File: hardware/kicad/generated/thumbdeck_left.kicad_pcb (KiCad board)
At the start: 4 copper layers, 75 x 98 mm, 85 parts, among them J2 FFC16, SW1 SNAP7, SW10 SNAP7, SW11 SNAP7, SW12 SNAP7, SW13 SNAP7, SW14 SNAP7, SW15 SNAP7, SW16 SNAP7, SW17 SNAP7, SW18 SNAP7, SW19 SNAP7, SW2 SNAP7, SW20 SNAP7, SW21 SNAP7, SW22 SNAP7, SW23 SNAP7, SW24 SNAP7, SW25 SNAP7, SW26 SNAP7, SW27 SNAP7, SW28 SNAP7, SW29 SNAP7, SW3 SNAP7, SW30 SNAP7, SW31 SNAP7, SW32 SNAP7, SW33 SNAP7, SW34 SNAP7, SW35 SNAP7, SW36 SNAP7, SW37 SNAP7, SW38 SNAP7, SW39 SNAP7, SW4 SNAP7, SW40 SNAP7, SW41 SNAP7, SW42 SNAP7, SW5 SNAP7, SW6 SNAP7, SW7 SNAP7, SW8 SNAP7, SW9 SNAP7

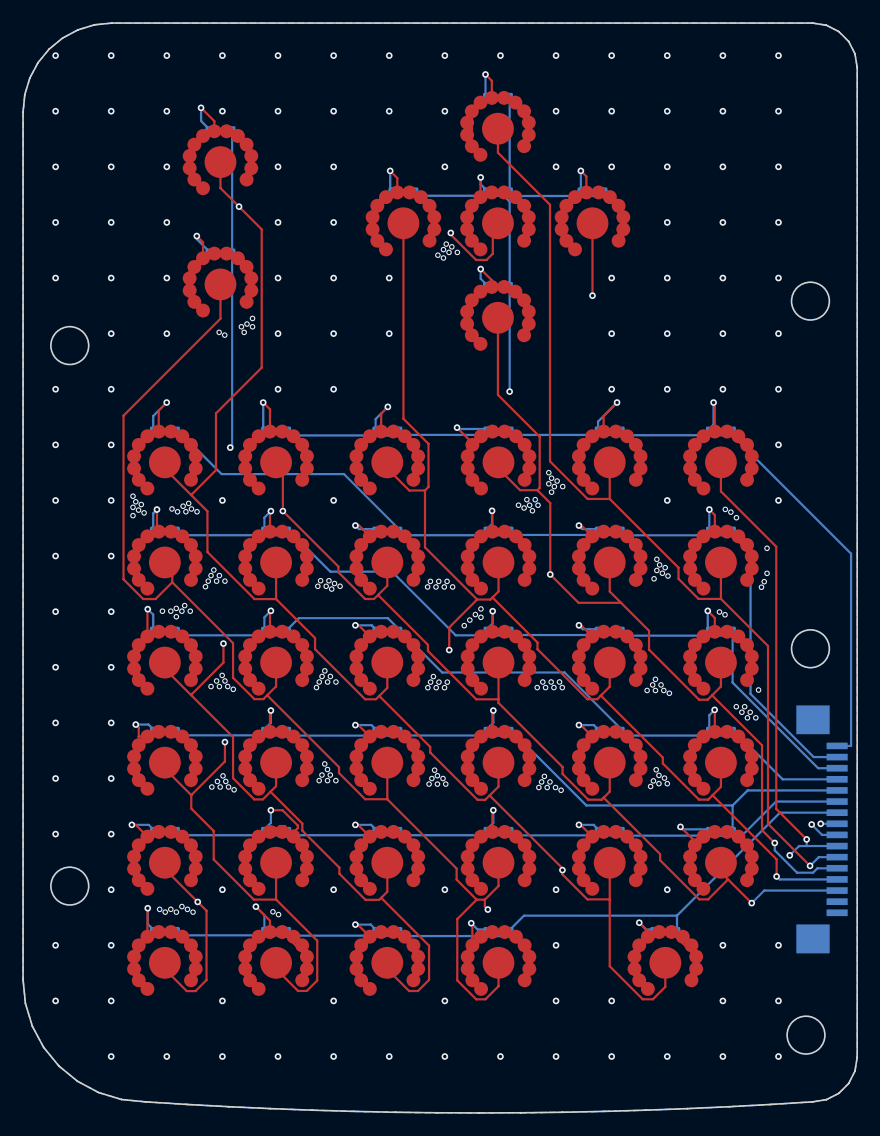
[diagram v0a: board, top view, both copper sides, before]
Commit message: v0.21: right-grip ThinkPad-style pointing nub — Bean-architecture TMAG5273 hall sensor
The right top zone mirrors the left cluster: PgUp/PgDn at the mouse-button
mirror, and a rate-control pointing nub at the exact D-pad mirror (32.3, 79.0).
Architecture per the Ploopy Bean (CERN-OHL-S v2, credited): a TMAG5273A1 I2C
hall sensor (C3716049, SOT-23-6, machine-placed SMT on the back) reads a
O4x2 N52 magnet in a printed flexure spring through the 1.6mm FR4; firmware
maps deflection to cursor VELOCITY (quadratic curve + deadzone + remainder).
An ALPS RKJXV gimbal variant was fully implemented first and rejected — the
11.2mm module body protruded through the face; recorded in the design log.

- board: U4 + R26/R27 pullups + C8 on the reserved TP6-8 I2C nets (P0.05/28/29),
  all-SMT again (71/43 placements); reworked USB In2 lane elbow; pre-placed GND
  escapes for U1.21/24 (fan-out walled their pour blob in deterministically);
  both boards routed 0 violations / 0 unconnected
- firmware: in-tree Zephyr module tmag5273_nub (Apache-2.0, register map from
  the upstream Zephyr driver, NOT the Bean's GPL QMK): 100Hz poll, boot zero
  calibration, DT-tunable curve, pm_device sleep hook (continuous mode would
  drain ~2.3mA through ZMK deep sleep); matrix stays 78 keys
- CAD: flat face with a O10 aperture; prints 8+9 = nub_spring (flange + spiral
  arms + legs clamped by the lid counterbore at 0.05 preload) and TPU nub_cap
  (4.25mm proud); 221 bodies, 0 collisions; GLB includes the nub
- docs: BOM/assembly/README/design-log rewritten for the nub; magnet polarity
  procedure; CI marked stale pending a v0.21 re-run; 78-key counts restored
- verified by a 17-agent adversarial review: fixed the spigot z-stack (cap had
  0.15mm engagement), the unclamped spring flange, and the sensor sleep drain

Co-Authored-By: Claude Fable 5 <noreply@anthropic.com>
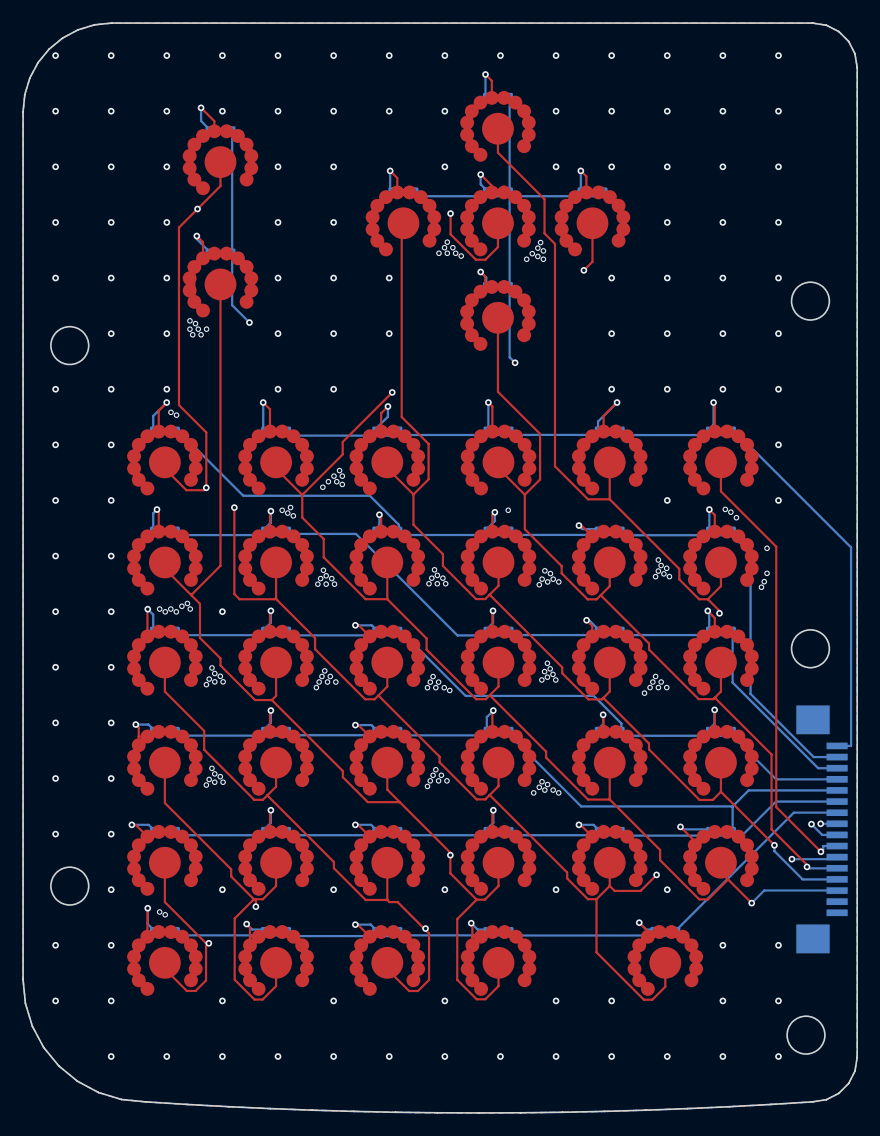
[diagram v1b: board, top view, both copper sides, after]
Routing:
- net COL8: track 167.0 -> 180.5 mm, vias 3 -> 2
- net ROW8: track 99.5 -> 90.3 mm
- net DN_L29: track 22.2 -> 17.7 mm
- net COL7: track 171.5 -> 167.6 mm, vias 3 -> 2
- net COL6: track 227.5 -> 223.8 mm, vias 2 -> 3
- net COL9: track 195.2 -> 191.7 mm
- net COL5: track 214.0 -> 217.3 mm, vias 5 -> 6
- net DN_L34: track 19.4 -> 17.3 mm
- net ROW6: track 66.4 -> 65.6 mm
- net DN_L38: track 17.4 -> 16.6 mm
- net DN_L10: track 17.4 -> 16.8 mm
- net DN_L14: track 17.2 -> 16.6 mm
- net DN_L36: track 16.9 -> 17.4 mm
- net GND: vias 304 -> 261

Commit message: v0.22: true-mirror page keys + genuine-TrackPoint-cap nub mount
Two feedback items on the v0.21 print:

- PGUP/PGDN move to the TRUE mouse-button mirror x=57.25 (the F10|DEL gap,
  mirroring the left pair's ESC|F1 gap; was 45.7, "above F9"). v0.21's
  blocker was a face-conflation: domes are front-side, the E73 is back-side —
  they coexist. Both feature diodes drop to deck y73.2 under the TP row
  (defaults hit the module belly / the SWD row), SW91 moves to the vacated
  old-PGUP zone (46.0, 80.5). Both boards re-route 0/0 on the first 40-pass
  attempt; fab re-exported (71/43); sim 78 keys PASS; firmware byte-identical.
- The nub becomes compatible with genuine ThinkPad caps: the spring's post is
  the classic-cap standard 4.4mm-square x 2.5 platform (classic full-size
  caps: ~4.5mm square socket, dims cross-checked against navcaps' printed
  cap mounts), and the printed cap is a classic soft-dome replica in
  ThinkPad-RED TPU (O7.8 mushroom, dot grid, same socket) — printed and
  genuine caps interchange. Hub top drops to z14.0 so the cap skirt nestles
  into the O10 aperture like a real TrackPoint; first tilt-stop is now the
  rubber skirt (gentler on the flexure). GLB paints it trackpoint_red.
- verify_alignment.py taught the v0.22 topology (DIODE_DECK overrides +
  side-aware courtyard check) — gate back to ALL CHECKS PASS.
- Adversarial review (13 agents) fixes folded in: cap waist O6.2->O6.8 (the
  socket corner left a 0.10mm unprintable wall at the waist — now 0.40mm),
  stale intermediate coordinates in the design log, stale doc claims.

Co-Authored-By: Claude Fable 5 <noreply@anthropic.com>
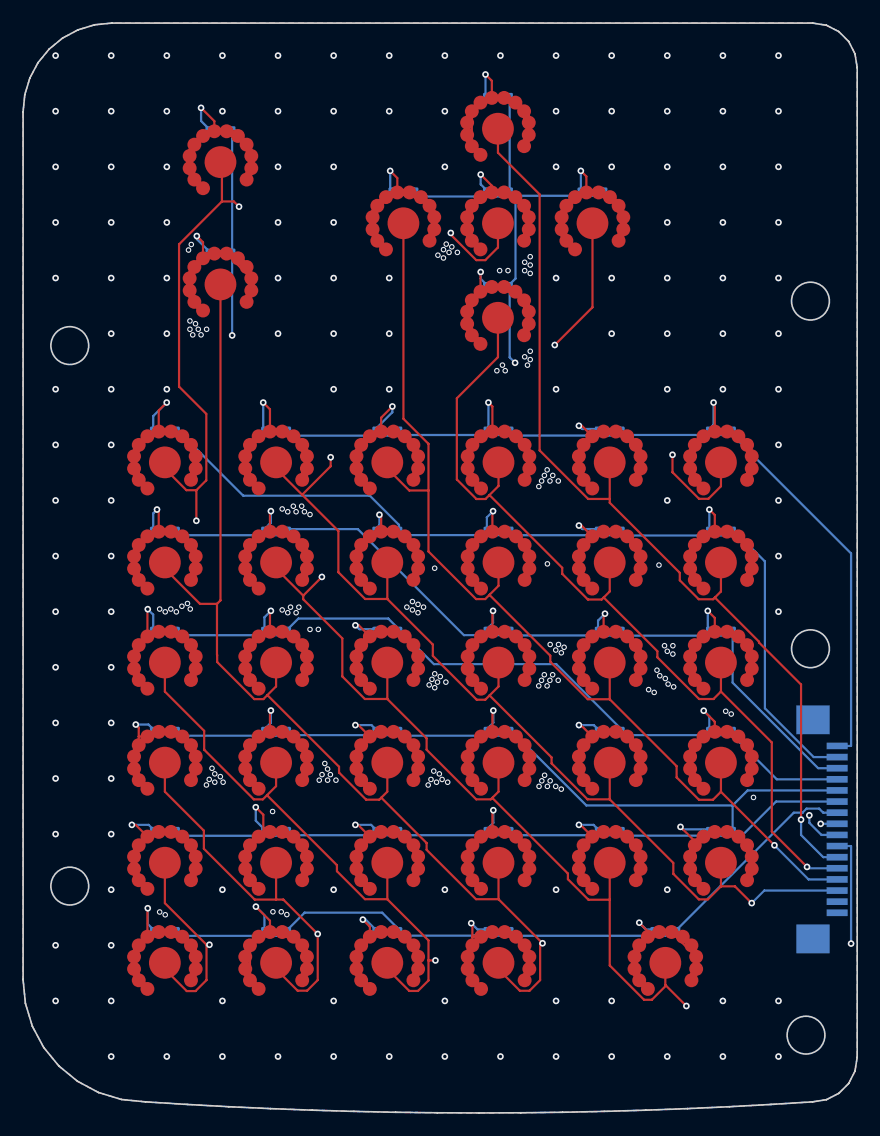
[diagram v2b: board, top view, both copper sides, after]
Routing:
- net COL6: track 223.8 -> 216.4 mm, vias 3 -> 2
- net COL5: track 217.3 -> 223.5 mm, vias 6 -> 7
- net COL8: track 180.5 -> 175.4 mm
- net ROW8: track 90.3 -> 93.7 mm
- net COL7: track 167.6 -> 170.7 mm
- net DN_L2: track 20.0 -> 17.2 mm
- net COL9: track 191.7 -> 194.4 mm
- net DN_L34: track 17.3 -> 19.4 mm
- net ROW6: track 65.6 -> 66.7 mm
- net DN_L29: track 17.7 -> 18.6 mm
- net DN_L33: track 17.5 -> 16.9 mm
- net GND: vias 261 -> 260
